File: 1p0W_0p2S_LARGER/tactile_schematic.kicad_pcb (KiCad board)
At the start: 2 copper layers, 145.2 x 85.6 mm, 55 parts, among them IC1 CY8C4145PVI-PS431, J1 Conn_01x03, J2 Conn_01x04, J3 Conn_01x04, J4 Conn_01x03, J5 Conn_ARM_SWD_TagConnect_TC203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

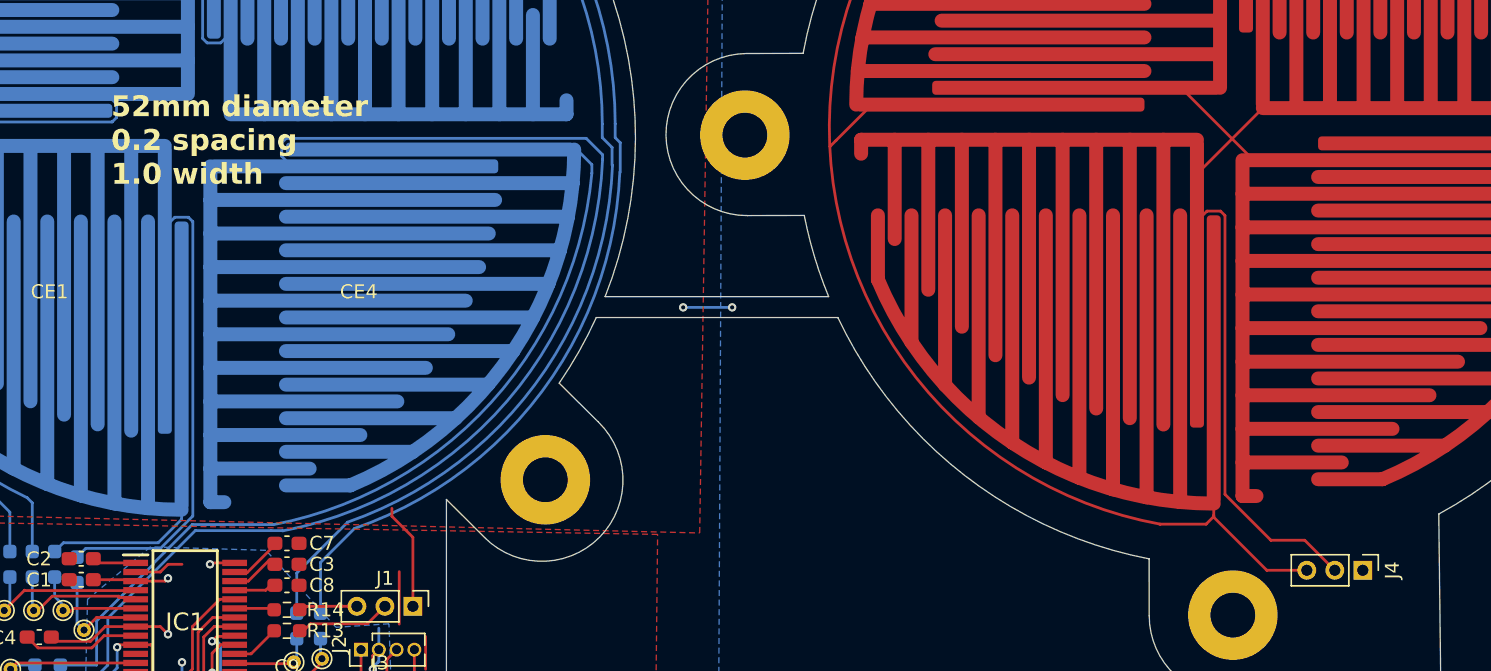
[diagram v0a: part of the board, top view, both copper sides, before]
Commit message: fixed silkscreen
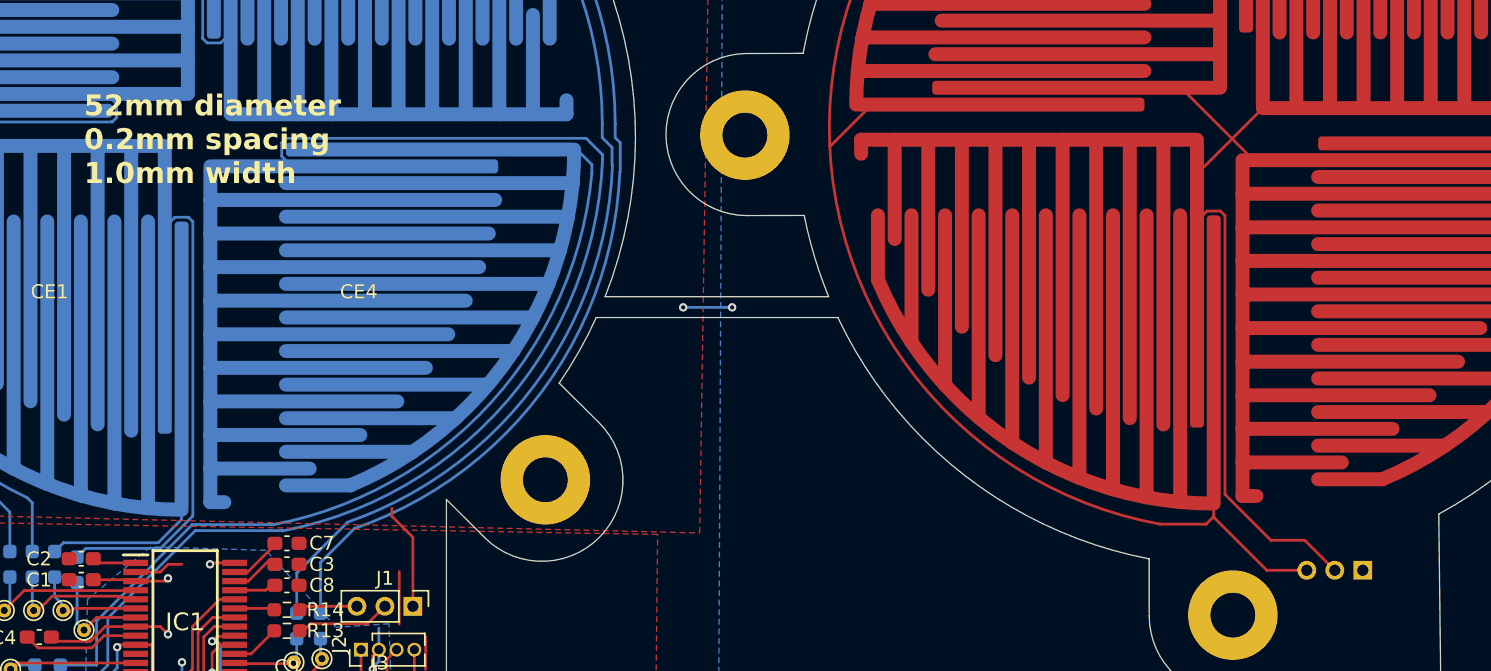
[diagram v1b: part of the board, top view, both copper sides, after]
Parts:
- J4: moved to B.Cu
- turned J4 to 90 degrees
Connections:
- net SHEILD renamed SHIELD
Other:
- board text added: "52mm diameter 0.2mm spacing 1.0mm width"
- board text removed: "52mm diameter 0.2 spacing 1.0 width"

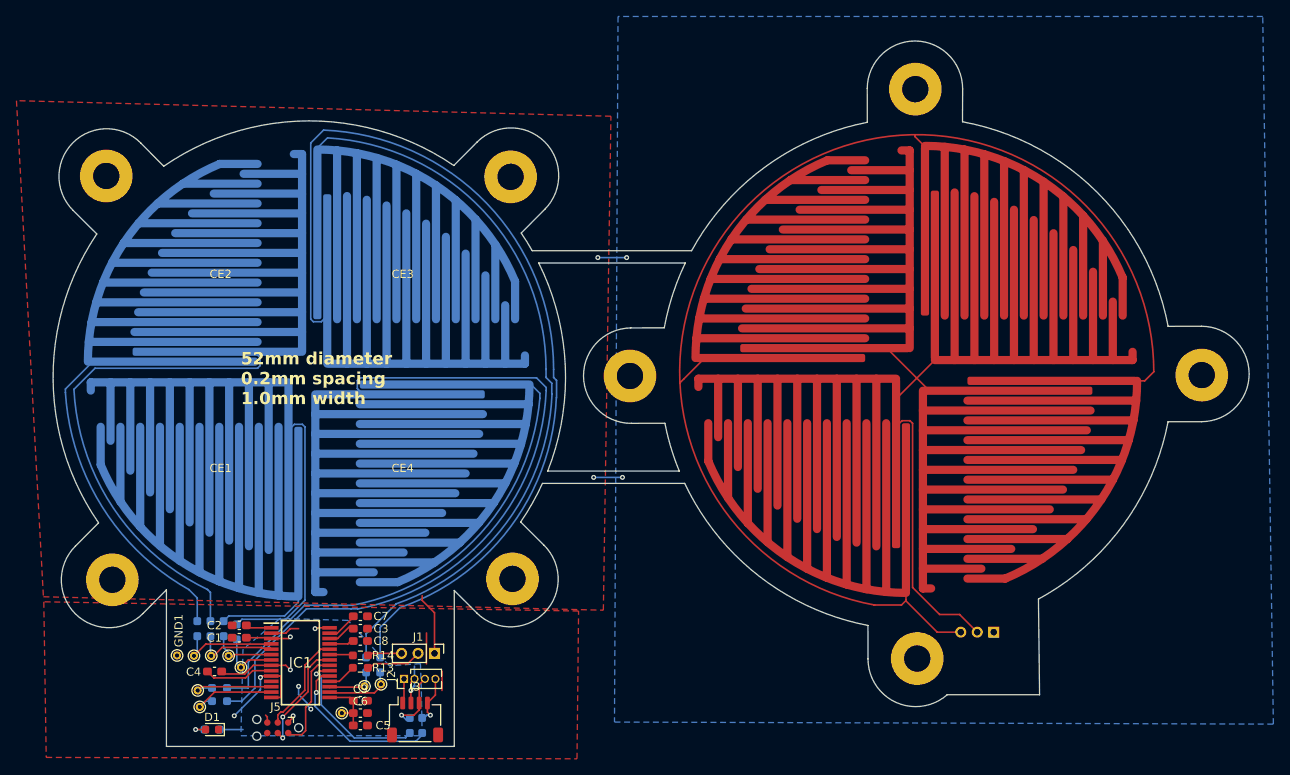
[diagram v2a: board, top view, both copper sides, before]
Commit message: last sizing + pin2.7 changes
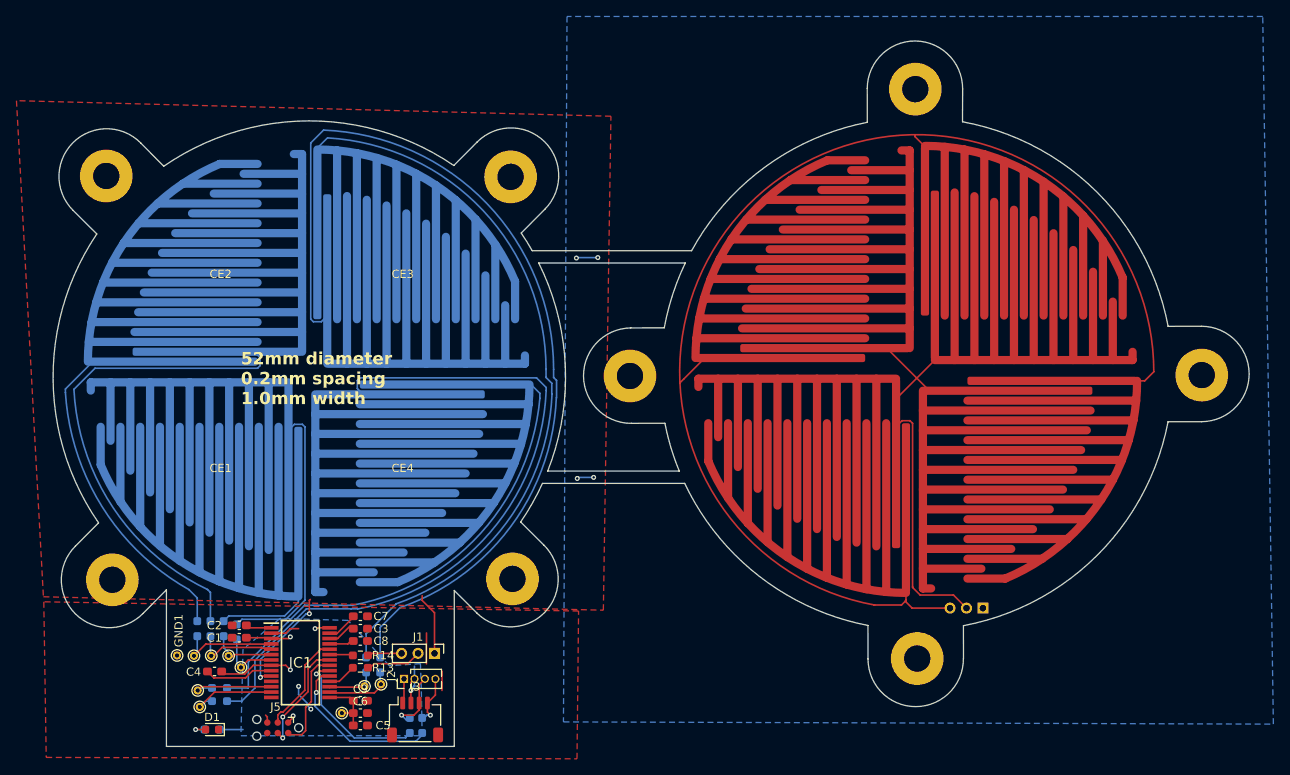
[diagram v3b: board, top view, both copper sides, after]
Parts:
- moved J4 3.20 mm to (197.2, 112.5)
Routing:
- net Net-(J1-Pin_3): track 74.8 -> 72.2 mm
- net Net-(J1-Pin_2): track 128.5 -> 126.0 mm
- net SHIELD: track 26.8 -> 25.9 mm
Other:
- outline, holes or cut-outs redrawn
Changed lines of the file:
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@@
 	(footprint "Connector_PinHeader_2.00mm:PinHeader_1x03_P2.00mm_Vertical"
 		(layer "B.Cu")
-		(at 198.455208 115.421992 90)
+		(at 197.150001 112.5 90)
 		(descr "Through hole straight pin header, 1x03, 2.00mm pitch, single row")
 		(tags "Through hole pin header THT 1x03 2.00mm single row")
@@
 	)
 	(gr_line
+		(start 194.783067 118.643513)
+		(end 194.7777 114.635439)
+		(stroke
+			(width 0.076)
+			(type default)
+		)
+		(layer "Edge.Cuts")
+	)
+	(gr_line
 		(start 89.795118 102.152737)
 		(end 86.978563 104.98596)
@@
 	(gr_arc
 		(start 219.613758 89.883864)
-		(mid 214.17166 102.414952)
-		(end 203.884742 111.405164)
+		(mid 211.015976 106.092876)
+		(end 194.7777 114.635259)
 		(stroke
 			(width 0.076)
@@
 	)
 	(gr_line
-		(start 204.022001 123.020583)
-		(end 203.884742 111.405164)
-		(stroke
-			(width 0.076)
-			(type default)
-		)
-		(layer "Edge.Cuts")
-	)
-	(gr_line
 		(start 135.756738 55.919088)
 		(end 132.916505 58.776131)
@@
 		(layer "Edge.Cuts")
 	)
-	(gr_line
-		(start 192.807244 123.020583)
-		(end 204.022001 123.020583)
-		(stroke
-			(width 0.076)
-			(type default)
-		)
-		(layer "Edge.Cuts")
-	)
 	(gr_arc
 		(start 97.70877 58.864942)
@@
 	)
 	(gr_arc
-		(start 192.807244 123.020583)
-		(mid 186.596346 123.946133)
+		(start 194.775686 118.642159)
+		(mid 188.997684 124.461431)
 		(end 183.193351 118.668423)
 		(stroke
@@
 	)
 	(segment
-		(start 194.455208 115.421992)
-		(end 191.59647 115.421992)
+		(start 187.717908 111.667908)
+		(end 187.25969 112.126125)
 		(width 0.2)
 		(layer "F.Cu")
@@
 	)
 	(segment
+		(start 188.55 112.5)
+		(end 193.150001 112.5)
+		(width 0.2)
+		(layer "F.Cu")
+		(net 21)
+	)
+	(segment
 		(start 187.805603 111.516125)
 		(end 187.805603 111.580212)
@@
 	)
 	(segment
-		(start 187.805603 111.631125)
-		(end 187.805603 111.516125)
-		(width 0.2)
-		(layer "F.Cu")
-		(net 21)
-	)
-	(segment
 		(start 160.82 84.7)
 		(end 160.38 85.14)
@@
 	)
 	(segment
-		(start 191.59647 115.421992)
-		(end 187.805603 111.631125)
+		(start 188.9 55.27)
+		(end 188.9 55.14)
 		(width 0.2)
 		(layer "F.Cu")
@@
 	)
 	(segment
-		(start 188.9 55.27)
-		(end 188.9 55.14)
+		(start 187.717908 111.667908)
+		(end 188.55 112.5)
 		(width 0.2)
 		(layer "F.Cu")
@@
 	(segment
 		(start 187.805603 111.580212)
-		(end 187.25969 112.126125)
+		(end 187.717908 111.667908)
 		(width 0.2)
 		(layer "F.Cu")
@@
 	)
 	(segment
+		(start 188.606603 109.9)
+		(end 188.606603 109.99491)
+		(width 0.2)
+		(layer "F.Cu")
+		(net 41)
+	)
+	(segment
+		(start 193.567125 110.917125)
+		(end 195.15 112.5)
+		(width 0.2)
+		(layer "F.Cu")
+		(net 41)
+	)
+	(segment
 		(start 186.605603 87.100272)
 		(end 186.605603 94.942125)
@@
 	)
 	(segment
-		(start 188.606603 109.99491)
+		(start 188.606603 109.9)
 		(end 188.606603 90.070965)
 		(width 0.2)
@@
 	)
 	(segment
-		(start 122.495423 120.006327)
-		(end 123.255625 119.246125)
-		(width 0.2)
-		(layer "F.Cu")
-		(net 41)
-	)
-	(segment
-		(start 188.606603 90.070965)
-		(end 188.290763 89.755125)
+		(start 188.606603 109.99491)
+		(end 189.528818 110.917125)
 		(width 0.2)
 		(layer "F.Cu")
@@
 	)
 	(segment
-		(start 194.30934 113.276125)
-		(end 191.887818 113.276125)
+		(start 122.495423 120.006327)
+		(end 123.255625 119.246125)
 		(width 0.2)
 		(layer "F.Cu")
@@
 	)
 	(segment
-		(start 191.887818 113.276125)
-		(end 188.606603 109.99491)
+		(start 188.606603 90.070965)
+		(end 188.290763 89.755125)
 		(width 0.2)
 		(layer "F.Cu")
@@
 	)
 	(segment
-		(start 196.455207 115.421992)
-		(end 194.30934 113.276125)
-		(width 0.2)
-		(layer "F.Cu")
-		(net 41)
-	)
-	(segment
 		(start 123.255625 119.246125)
 		(end 127.325603 119.246125)
@@
 	)
 	(segment
+		(start 189.528818 110.917125)
+		(end 193.567125 110.917125)
+		(width 0.2)
+		(layer "F.Cu")
+		(net 41)
+	)
+	(segment
 		(start 102.788102 127.246125)
 		(end 101.575603 127.246125)
@@
 	)
 	(segment
-		(start 110.761108 120.746125)
-		(end 111.848608 120.746125)
-		(width 0.2)
-		(layer "F.Cu")
-		(net 45)
-	)
-	(segment
 		(start 109.614261 120.746125)
 		(end 109.442452 120.917934)
@@
 	)
 	(segment
-		(start 110.761108 120.746125)
-		(end 109.614261 120.746125)
-		(width 0.2)
-		(layer "F.Cu")
-		(net 45)
-	)
-	(segment
-		(start 111.848608 120.746125)
-		(end 111.949608 120.847125)
-		(width 0.2)
-		(layer "F.Cu")
-		(net 45)
-	)
-	(segment
-		(start 111.848608 123.346125)
-		(end 110.761108 123.346125)
+		(start 115.382629 111.567371)
+		(end 115.5 111.45)
 		(width 0.2)
 		(layer "F.Cu")
@@
 	)
 	(segment
-		(start 111.949608 123.245125)
-		(end 111.848608 123.346125)
+		(start 110.761108 120.746125)
+		(end 109.614261 120.746125)
 		(width 0.2)
 		(layer "F.Cu")
@@
 	)
 	(segment
-		(start 111.949608 120.847125)
-		(end 111.949608 123.245125)
+		(start 130.575603 113.065824)
+		(end 129.075603 111.565825)
 		(width 0.2)
 		(layer "F.Cu")
@@
 	)
 	(segment
-		(start 130.575603 113.065824)
-		(end 129.075603 111.565825)
+		(start 115.382629 113.186125)
+		(end 115.382629 111.567371)
 		(width 0.2)
 		(layer "F.Cu")
@@
 	)
 	(via
-		(at 153.390603 96.636125)
+		(at 147.9 96.763487)
 		(size 0.6)
 		(drill 0.3)
@@
 	)
 	(via
-		(at 106.265603 125.576125)
+		(at 115.382629 113.186125)
 		(size 0.6)
 		(drill 0.3)
@@
 	)
 	(via
-		(at 153.900603 69.956125)
+		(at 147.8 70.010357)
 		(size 0.6)
 		(drill 0.3)
@@
 	)
 	(segment
-		(start 109.442452 122.399276)
-		(end 109.442452 120.917934)
+		(start 148.027362 96.636125)
+		(end 149.890603 96.636125)
 		(width 0.2)
 		(layer "B.Cu")
@@
 	)
 	(segment
-		(start 150.400603 69.956125)
-		(end 153.900603 69.956125)
+		(start 147.9 96.763487)
+		(end 148.027362 96.636125)
 		(width 0.2)
 		(layer "B.Cu")
@@
 	)
 	(segment
-		(start 106.265603 125.576125)
-		(end 109.442452 122.399276)
+		(start 114.997703 113.186125)
+		(end 109.442452 118.741376)
 		(width 0.2)
 		(layer "B.Cu")
@@
 	)
 	(segment
-		(start 153.390603 96.636125)
-		(end 149.890603 96.636125)
+		(start 115.382629 113.186125)
+		(end 114.997703 113.186125)
+		(width 0.2)
+		(layer "B.Cu")
+		(net 45)
+	)
+	(segment
+		(start 109.442452 118.741376)
+		(end 109.442452 120.917934)
+		(width 0.2)
+		(layer "B.Cu")
+		(net 45)
+	)
+	(segment
+		(start 147.854232 69.956125)
+		(end 147.8 70.010357)
+		(width 0.2)
+		(layer "B.Cu")
+		(net 45)
+	)
+	(segment
+		(start 150.400603 69.956125)
+		(end 147.854232 69.956125)
 		(width 0.2)
 		(layer "B.Cu")
@@
 		(hatch edge 0.5)
 		(connect_pads
-			(clearance 0.5)
+			(clearance 0.35)
 		)
-		(min_thickness 0.25)
+		(min_thickness 0.2)
 		(filled_areas_thickness no)
 		(fill yes
-			(thermal_gap 0.5)
+			(thermal_gap 0.4)
 			(thermal_bridge_width 0.5)
 		)
@@
 		(polygon
 			(pts
-				(xy 152.850603 40.686125) (xy 152.420603 126.336125) (xy 232.400603 126.586125) (xy 231.110603 40.686125)
+				(xy 146.657631 40.686125) (xy 146.227728 126.316768) (xy 232.400603 126.586125) (xy 231.110603 40.686125)
 			)
 		)
